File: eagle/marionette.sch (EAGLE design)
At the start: 225 parts, among them J17 MA02-1, J18 MA02-1, J19 MA02-1, J2 SWD, J20 MA02-1, J22 ZX62D-B-5P8, J6 MA03-2W, J8 MA04-2W, Q1 BSS84, U1 STM32F407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

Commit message: Connected USB_FS_VBUS to V_USB Added 0ohm resistor to ULPI did more stuff....cant remember
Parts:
- added R38: 0, rcl_custom:R-US_0603-C
- added R63: 10k, rcl_custom:R-US_0603-C
- LED1: value (none) -> RGB
- R15: value 820 -> 10k
- U14: value (none) -> USB3320
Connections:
- removed net FS_ID: U1G$1.PA10
- removed net PD5: U1G$4.PD5
- removed net PI10: U1G$9.PI10
- new net N$2: R38.2, U14.XO
- net GND: now also R63.2
- net PB14: now also R38.1
- net PB4: now also R63.1

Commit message: fixed the 0ohm resistor to ULPI
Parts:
- added V_USB: TEST-POINT10MIL-TEST-POINT, Tova:TEST-POINT10MIL-TEST-POINT
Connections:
- removed net N$47: C32.1, D4.A, J22.VCC, R15.1
- new net V_USB: C32.1, D4.A, J22.VCC, R15.1, U1G$1.PA9, V_USB.1
- net 3.3VDD: no longer U1G$1.PA9
- net N$2: now also R38.1, U14.XI; no longer R38.2, U14.XO
- net PB14: now also R38.2; no longer R38.1, U14.XI
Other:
- moved on the sheet: R38
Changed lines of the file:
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@@
 <part name="D28" library="ESD8008MUT" deviceset="ESD8008" device=""/>
 <part name="GND53" library="GROUND" deviceset="GND" device=""/>
-<part name="U$39" library="3_3VDDsupply" deviceset="3.3VDD" device=""/>
 <part name="S2" library="PTS645" deviceset="PTS645" device=""/>
 <part name="C83" library="rcl_custom" deviceset="C-EU" device="0603-C" value="100nF, 10V"/>
@@
 <part name="R63" library="rcl_custom" deviceset="R-US_" device="0603-C" value="10k"/>
 <part name="GND34" library="GROUND" deviceset="GND" device=""/>
+<part name="V_USB" library="Tova" deviceset="TEST-POINT" device="10MIL-TEST-POINT"/>
 </parts>
 <sheets>
@@
 <attribute name="NAME" x="321.945" y="90.805" size="1.778" layer="95" font="vector"/>
 </instance>
-<instance part="U$39" gate="3.3VDD" x="187.96" y="351.79"/>
 <instance part="U12" gate="G$1" x="270.51" y="205.74"/>
 <instance part="GND57" gate="1" x="270.51" y="181.61"/>
@@
 <attribute name="NAME" x="167.005" y="353.695" size="1.778" layer="95" font="vector"/>
 </instance>
-<instance part="R38" gate="R" x="407.67" y="386.08"/>
+<instance part="R38" gate="R" x="398.78" y="382.27" rot="R180"/>
 <instance part="R63" gate="R" x="341.63" y="347.98" rot="R270"/>
 <instance part="GND34" gate="1" x="341.63" y="339.09"/>
+<instance part="V_USB" gate="G$1" x="476.25" y="351.79" smashed="yes">
+<attribute name="NAME" x="474.345" y="353.695" size="1.778" layer="95" font="vector"/>
+</instance>
 </instances>
 <busses>
@@
 </segment>
 </bus>
-<bus name="USB_FS_BUS:FS_P,FS_N">
+<bus name="USB_FS_BUS:V_USB,FS_P,FS_N">
 <segment>
 <wire x1="201.93" y1="328.93" x2="201.93" y2="367.03" width="0.762" layer="92"/>
@@
 </segment>
 <segment>
-<pinref part="U14" gate="U" pin="XI"/>
-<wire x1="405.13" y1="377.19" x2="405.13" y2="381" width="0.1524" layer="91"/>
-<wire x1="405.13" y1="381" x2="402.59" y2="381" width="0.1524" layer="91"/>
-<label x="394.97" y="381" size="1.778" layer="95" rot="R180" xref="yes"/>
-<pinref part="R38" gate="R" pin="1"/>
-<wire x1="402.59" y1="381" x2="394.97" y2="381" width="0.1524" layer="91"/>
-<wire x1="402.59" y1="381" x2="402.59" y2="386.08" width="0.1524" layer="91"/>
-<junction x="402.59" y="381"/>
+<label x="392.43" y="382.27" size="1.778" layer="95" rot="R180" xref="yes"/>
+<pinref part="R38" gate="R" pin="2"/>
+<wire x1="392.43" y1="382.27" x2="393.7" y2="382.27" width="0.1524" layer="91"/>
 </segment>
 </net>
@@
 </segment>
 <segment>
-<pinref part="U1" gate="G$1" pin="PA9"/>
-<wire x1="107.95" y1="346.71" x2="186.69" y2="346.71" width="0.1524" layer="91"/>
-<label x="129.54" y="346.71" size="1.778" layer="95"/>
-<wire x1="186.69" y1="346.71" x2="187.96" y2="347.98" width="0.1524" layer="91"/>
-<pinref part="U$39" gate="3.3VDD" pin="3.3VDD"/>
-<wire x1="187.96" y1="347.98" x2="187.96" y2="349.25" width="0.1524" layer="91"/>
-</segment>
-<segment>
 <pinref part="U$30" gate="3.3VDD" pin="3.3VDD"/>
 <pinref part="C28" gate="CE" pin="1"/>
@@
 <pinref part="U14" gate="U" pin="S1"/>
 <wire x1="420.37" y1="389.89" x2="420.37" y2="377.19" width="0.1524" layer="91"/>
-<wire x1="420.37" y1="389.89" x2="383.54" y2="389.89" width="0.1524" layer="91"/>
+<wire x1="420.37" y1="389.89" x2="382.27" y2="389.89" width="0.1524" layer="91"/>
 <pinref part="U14" gate="U" pin="3.3V"/>
-<wire x1="383.54" y1="389.89" x2="379.73" y2="389.89" width="0.1524" layer="91"/>
+<wire x1="382.27" y1="389.89" x2="379.73" y2="389.89" width="0.1524" layer="91"/>
 <wire x1="379.73" y1="389.89" x2="373.38" y2="389.89" width="0.1524" layer="91"/>
 <wire x1="373.38" y1="389.89" x2="365.76" y2="389.89" width="0.1524" layer="91"/>
-<wire x1="387.35" y1="367.03" x2="383.54" y2="367.03" width="0.1524" layer="91"/>
-<wire x1="383.54" y1="367.03" x2="383.54" y2="369.57" width="0.1524" layer="91"/>
+<wire x1="387.35" y1="367.03" x2="382.27" y2="367.03" width="0.1524" layer="91"/>
+<wire x1="382.27" y1="367.03" x2="382.27" y2="369.57" width="0.1524" layer="91"/>
 <pinref part="U14" gate="U" pin="VBAT"/>
-<wire x1="383.54" y1="369.57" x2="387.35" y2="369.57" width="0.1524" layer="91"/>
-<wire x1="383.54" y1="369.57" x2="383.54" y2="389.89" width="0.1524" layer="91"/>
-<junction x="383.54" y="369.57"/>
-<junction x="383.54" y="389.89"/>
+<wire x1="382.27" y1="369.57" x2="387.35" y2="369.57" width="0.1524" layer="91"/>
+<wire x1="382.27" y1="369.57" x2="382.27" y2="389.89" width="0.1524" layer="91"/>
+<junction x="382.27" y="369.57"/>
+<junction x="382.27" y="389.89"/>
 <pinref part="U14" gate="U" pin="VIO"/>
 <wire x1="387.35" y1="361.95" x2="379.73" y2="361.95" width="0.1524" layer="91"/>
@@
 </segment>
 </net>
-<net name="N$47" class="0">
-<segment>
+<net name="PD7" class="0">
+<segment>
+<wire x1="173.99" y1="77.47" x2="171.45" y2="74.93" width="0.1524" layer="91"/>
+<pinref part="U1" gate="G$4" pin="PD7"/>
+<wire x1="171.45" y1="74.93" x2="107.95" y2="74.93" width="0.1524" layer="91"/>
+</segment>
+</net>
+<net name="V_USB" class="0">
+<segment>
+<wire x1="201.93" y1="349.25" x2="199.39" y2="346.71" width="0.1524" layer="91"/>
+<pinref part="U1" gate="G$1" pin="PA9"/>
+<wire x1="199.39" y1="346.71" x2="107.95" y2="346.71" width="0.1524" layer="91"/>
+<label x="129.54" y="346.71" size="1.778" layer="95"/>
+</segment>
+<segment>
+<wire x1="452.12" y1="331.47" x2="453.39" y2="330.2" width="0.1524" layer="91"/>
+<wire x1="453.39" y1="330.2" x2="474.98" y2="330.2" width="0.1524" layer="91"/>
+<wire x1="474.98" y1="330.2" x2="476.25" y2="331.47" width="0.1524" layer="91"/>
 <pinref part="D4" gate="G$1" pin="A"/>
 <wire x1="505.46" y1="369.57" x2="497.84" y2="369.57" width="0.1524" layer="91"/>
@@
 <wire x1="487.68" y1="367.03" x2="487.68" y2="369.57" width="0.1524" layer="91"/>
 <junction x="487.68" y="369.57"/>
-</segment>
-</net>
-<net name="PD7" class="0">
-<segment>
-<wire x1="173.99" y1="77.47" x2="171.45" y2="74.93" width="0.1524" layer="91"/>
-<pinref part="U1" gate="G$4" pin="PD7"/>
-<wire x1="171.45" y1="74.93" x2="107.95" y2="74.93" width="0.1524" layer="91"/>
+<wire x1="476.25" y1="331.47" x2="476.25" y2="351.79" width="0.1524" layer="91"/>
+<junction x="476.25" y="351.79"/>
+<label x="457.2" y="330.2" size="1.778" layer="95"/>
+<pinref part="V_USB" gate="G$1" pin="1"/>
 </segment>
 </net>
 <net name="N$2" class="0">
 <segment>
-<pinref part="U14" gate="U" pin="XO"/>
-<pinref part="R38" gate="R" pin="2"/>
-<wire x1="412.75" y1="377.19" x2="412.75" y2="386.08" width="0.1524" layer="91"/>
-</segment>
-</net>
+<pinref part="R38" gate="R" pin="1"/>
+<wire x1="403.86" y1="382.27" x2="405.13" y2="382.27" width="0.1524" layer="91"/>
+<pinref part="U14" gate="U" pin="XI"/>
+<wire x1="405.13" y1="382.27" x2="405.13" y2="377.19" width="0.1524" layer="91"/>
+</segment>
+</net>

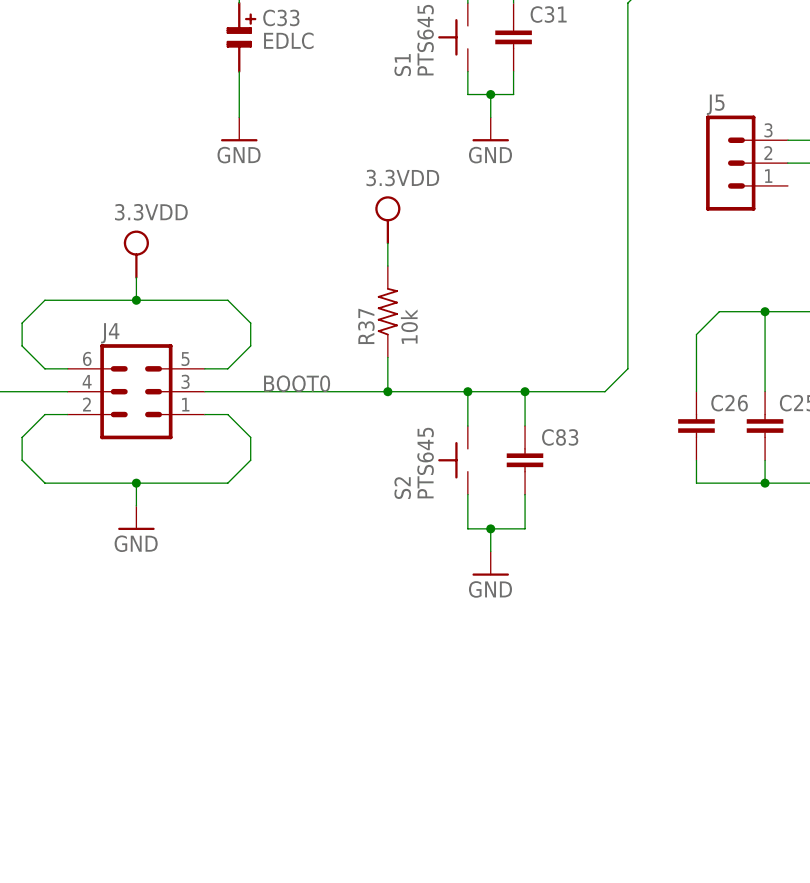
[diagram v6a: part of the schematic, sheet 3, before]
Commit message: fixed boot0 switch for DFU
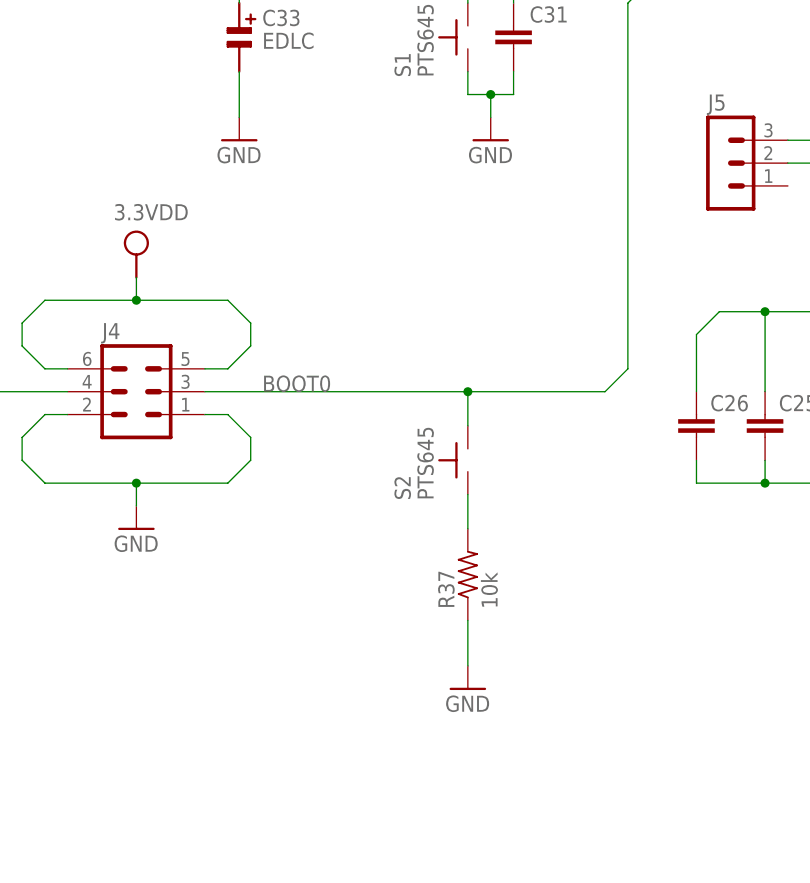
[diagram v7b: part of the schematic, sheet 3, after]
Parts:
- removed C83: 100nF, 10V, rcl_custom:C-EU0603-C
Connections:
- new net N$37: R37.2, S2.P$1
- net 3.3VDD: no longer R37.2
- net BOOT0: no longer C83.1, R37.1
- net GND: now also R37.1; no longer C83.2, S2.P$1
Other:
- moved on the sheet: R37
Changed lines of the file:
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@@
 <part name="GND53" library="GROUND" deviceset="GND" device=""/>
 <part name="S2" library="PTS645" deviceset="PTS645" device=""/>
-<part name="C83" library="rcl_custom" deviceset="C-EU" device="0603-C" value="100nF, 10V"/>
 <part name="GND54" library="GROUND" deviceset="GND" device=""/>
 <part name="SCL" library="Tova" deviceset="TEST-POINT" device="10MIL-TEST-POINT"/>
@@
 <part name="C84" library="rcl_custom" deviceset="C-EU" device="0603-C" value="NP"/>
 <part name="R37" library="rcl_custom" deviceset="R-US_" device="0603-C" value="10k"/>
-<part name="U$1" library="3_3VDDsupply" deviceset="3.3VDD" device=""/>
 <part name="U14" library="USB3320" deviceset="USB_PHY-SMSC-USB3320" device="-QFN32-5X5" value="USB3320"/>
 <part name="GND58" library="GROUND" deviceset="GND" device=""/>
@@
 </instance>
 <instance part="S2" gate="G$1" x="93.98" y="59.69" rot="R90"/>
-<instance part="C83" gate="CE" x="100.33" y="60.96" smashed="yes">
-<attribute name="NAME" x="106.426" y="63.119" size="1.778" layer="95" rot="R180"/>
-</instance>
-<instance part="GND54" gate="1" x="96.52" y="46.99"/>
-<instance part="R37" gate="R" x="85.09" y="76.2" rot="R90"/>
-<instance part="U$1" gate="3.3VDD" x="85.09" y="86.36"/>
+<instance part="GND54" gate="1" x="93.98" y="34.29"/>
+<instance part="R37" gate="R" x="93.98" y="46.99" rot="R90"/>
 </instances>
 <busses>
@@
 </segment>
 <segment>
-<pinref part="C83" gate="CE" pin="2"/>
-<wire x1="100.33" y1="55.88" x2="100.33" y2="52.07" width="0.1524" layer="91"/>
-<wire x1="100.33" y1="52.07" x2="96.52" y2="52.07" width="0.1524" layer="91"/>
-<pinref part="S2" gate="G$1" pin="P$1"/>
-<wire x1="96.52" y1="52.07" x2="93.98" y2="52.07" width="0.1524" layer="91"/>
-<wire x1="93.98" y1="52.07" x2="93.98" y2="55.88" width="0.1524" layer="91"/>
-<wire x1="96.52" y1="52.07" x2="96.52" y2="49.53" width="0.1524" layer="91"/>
+<wire x1="93.98" y1="41.91" x2="93.98" y2="36.83" width="0.1524" layer="91"/>
 <pinref part="GND54" gate="1" pin="GND"/>
-<junction x="96.52" y="52.07"/>
+<pinref part="R37" gate="R" pin="1"/>
 </segment>
 </net>
@@
 <net name="BOOT0" class="0">
 <segment>
-<wire x1="64.77" y1="67.31" x2="85.09" y2="67.31" width="0.1524" layer="91"/>
-<wire x1="85.09" y1="67.31" x2="93.98" y2="67.31" width="0.1524" layer="91"/>
-<wire x1="93.98" y1="67.31" x2="100.33" y2="67.31" width="0.1524" layer="91"/>
-<wire x1="100.33" y1="67.31" x2="109.22" y2="67.31" width="0.1524" layer="91"/>
+<wire x1="64.77" y1="67.31" x2="93.98" y2="67.31" width="0.1524" layer="91"/>
+<wire x1="93.98" y1="67.31" x2="109.22" y2="67.31" width="0.1524" layer="91"/>
 <wire x1="109.22" y1="67.31" x2="111.76" y2="69.85" width="0.1524" layer="91"/>
 <wire x1="111.76" y1="69.85" x2="111.76" y2="110.49" width="0.1524" layer="91"/>
@@
 <pinref part="S2" gate="G$1" pin="P$2"/>
 <wire x1="93.98" y1="63.5" x2="93.98" y2="67.31" width="0.1524" layer="91"/>
-<pinref part="C83" gate="CE" pin="1"/>
-<wire x1="100.33" y1="63.5" x2="100.33" y2="67.31" width="0.1524" layer="91"/>
 <junction x="93.98" y="67.31"/>
-<junction x="100.33" y="67.31"/>
-<pinref part="R37" gate="R" pin="1"/>
-<wire x1="85.09" y1="67.31" x2="85.09" y2="71.12" width="0.1524" layer="91"/>
-<junction x="85.09" y="67.31"/>
 </segment>
 </net>
@@
 <wire x1="171.45" y1="104.14" x2="171.45" y2="105.41" width="0.1524" layer="91"/>
 </segment>
-<segment>
-<pinref part="R37" gate="R" pin="2"/>
-<pinref part="U$1" gate="3.3VDD" pin="3.3VDD"/>
-<wire x1="85.09" y1="81.28" x2="85.09" y2="83.82" width="0.1524" layer="91"/>
-</segment>
 </net>
 <net name="N$6" class="0">
@@
 </segment>
 </net>
+<net name="N$37" class="0">
+<segment>
+<pinref part="S2" gate="G$1" pin="P$1"/>
+<wire x1="93.98" y1="52.07" x2="93.98" y2="55.88" width="0.1524" layer="91"/>
+<pinref part="R37" gate="R" pin="2"/>
+</segment>
+</net>

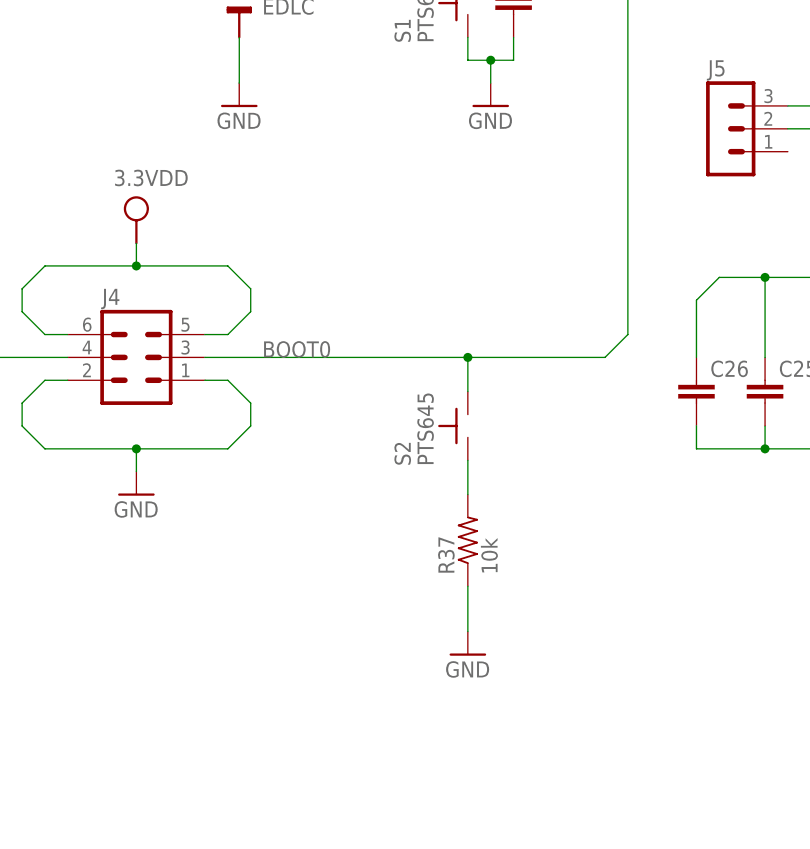
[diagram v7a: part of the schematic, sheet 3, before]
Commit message: now I really fixed switch for DFU
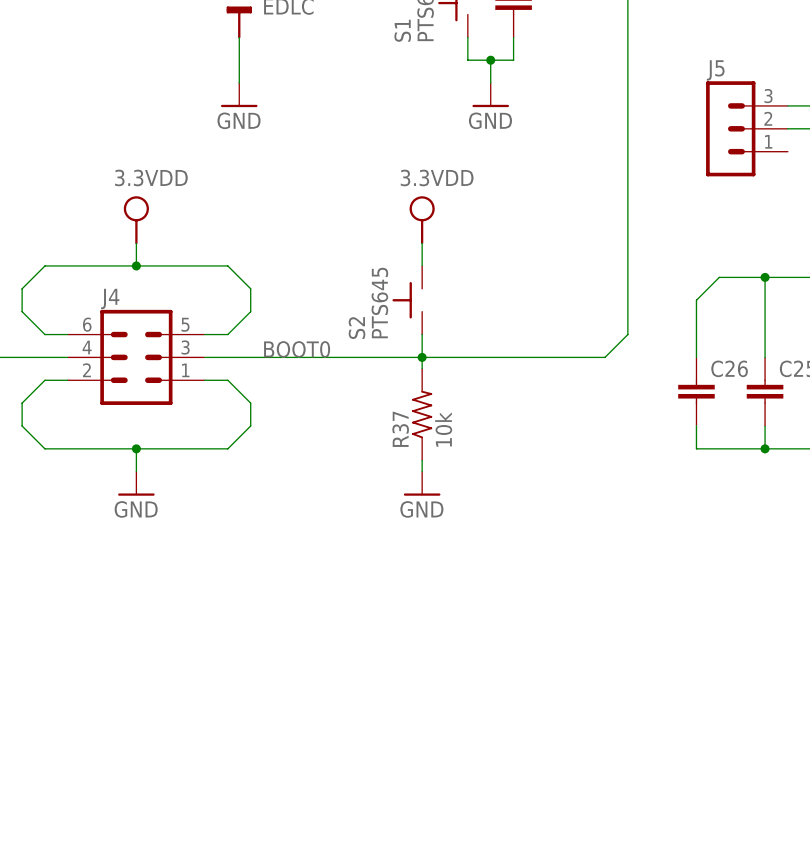
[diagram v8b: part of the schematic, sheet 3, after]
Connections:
- removed net N$37: R37.2, S2.P$1
- net 3.3VDD: now also S2.P$2
- net BOOT0: now also R37.2, S2.P$1; no longer S2.P$2
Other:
- moved on the sheet: R37, S2
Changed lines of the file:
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@@
 <part name="GND34" library="GROUND" deviceset="GND" device=""/>
 <part name="V_USB" library="Tova" deviceset="TEST-POINT" device="10MIL-TEST-POINT"/>
+<part name="U$1" library="3_3VDDsupply" deviceset="3.3VDD" device=""/>
 </parts>
 <sheets>
@@
 <attribute name="VALUE" x="173.99" y="107.95" size="1.778" layer="96"/>
 </instance>
-<instance part="S2" gate="G$1" x="93.98" y="59.69" rot="R90"/>
-<instance part="GND54" gate="1" x="93.98" y="34.29"/>
-<instance part="R37" gate="R" x="93.98" y="46.99" rot="R90"/>
+<instance part="S2" gate="G$1" x="88.9" y="73.66" rot="R90"/>
+<instance part="GND54" gate="1" x="88.9" y="52.07"/>
+<instance part="R37" gate="R" x="88.9" y="60.96" rot="R90"/>
+<instance part="U$1" gate="3.3VDD" x="88.9" y="82.55"/>
 </instances>
 <busses>
@@
 </segment>
 <segment>
-<wire x1="93.98" y1="41.91" x2="93.98" y2="36.83" width="0.1524" layer="91"/>
+<wire x1="88.9" y1="55.88" x2="88.9" y2="54.61" width="0.1524" layer="91"/>
 <pinref part="GND54" gate="1" pin="GND"/>
 <pinref part="R37" gate="R" pin="1"/>
@@
 <net name="BOOT0" class="0">
 <segment>
-<wire x1="64.77" y1="67.31" x2="93.98" y2="67.31" width="0.1524" layer="91"/>
-<wire x1="93.98" y1="67.31" x2="109.22" y2="67.31" width="0.1524" layer="91"/>
+<wire x1="64.77" y1="67.31" x2="88.9" y2="67.31" width="0.1524" layer="91"/>
+<wire x1="88.9" y1="67.31" x2="109.22" y2="67.31" width="0.1524" layer="91"/>
 <wire x1="109.22" y1="67.31" x2="111.76" y2="69.85" width="0.1524" layer="91"/>
 <wire x1="111.76" y1="69.85" x2="111.76" y2="110.49" width="0.1524" layer="91"/>
@@
 <label x="156.21" y="113.03" size="1.778" layer="95"/>
 <pinref part="J4" gate="1" pin="3"/>
-<pinref part="S2" gate="G$1" pin="P$2"/>
-<wire x1="93.98" y1="63.5" x2="93.98" y2="67.31" width="0.1524" layer="91"/>
-<junction x="93.98" y="67.31"/>
+<pinref part="S2" gate="G$1" pin="P$1"/>
+<wire x1="88.9" y1="67.31" x2="88.9" y2="69.85" width="0.1524" layer="91"/>
+<junction x="88.9" y="67.31"/>
+<pinref part="R37" gate="R" pin="2"/>
+<wire x1="88.9" y1="67.31" x2="88.9" y2="66.04" width="0.1524" layer="91"/>
 </segment>
 </net>
@@
 <wire x1="171.45" y1="104.14" x2="171.45" y2="105.41" width="0.1524" layer="91"/>
 </segment>
+<segment>
+<pinref part="S2" gate="G$1" pin="P$2"/>
+<wire x1="88.9" y1="77.47" x2="88.9" y2="80.01" width="0.1524" layer="91"/>
+<pinref part="U$1" gate="3.3VDD" pin="3.3VDD"/>
+</segment>
 </net>
 <net name="N$6" class="0">
@@
 </segment>
 </net>
-<net name="N$37" class="0">
-<segment>
-<pinref part="S2" gate="G$1" pin="P$1"/>
-<wire x1="93.98" y1="52.07" x2="93.98" y2="55.88" width="0.1524" layer="91"/>
-<pinref part="R37" gate="R" pin="2"/>
-</segment>
-</net>
